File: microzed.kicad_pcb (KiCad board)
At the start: 10 copper layers, 60 x 100 mm, 333 parts, among them IC1 XC7Z020-1CLG484C, IC2 RTL8211E-VL-CG, J1 640456-3, J2 10104111-0001LF, J3 L829-1J1T-43, J4 Micro_SD_Card_Det_Hirose_DM3AT, J5 10104111-0001LF, J6 BSH-090-01-X-D-A, J7 BSH-090-01-X-D-A, Q1 MMBT3904, Q2 MMBT3904, SW1 SW_Push, U1 TLV62130RGTR, U10 MT41K256M16TW, U11 MT25QL128ABA8E12-1SIT, U12 USB3320C-EZK, U13 ASDMB-24.000MHZ-LC-T, U14 ASDMB-25.000MHZ-LC-T, U15 TXS02612RTWR, U16 CP2104-F03-GM, U2 TLV62130RGTR, U3 TLV62130RGTR, U4 TLV62130RGTR, U5 TLV62130RGTR, U6 ASDMB-33.333MHZ-LC-T, U7 TPS51206DSQR, U8 REF3012, U9 MT41K256M16TW

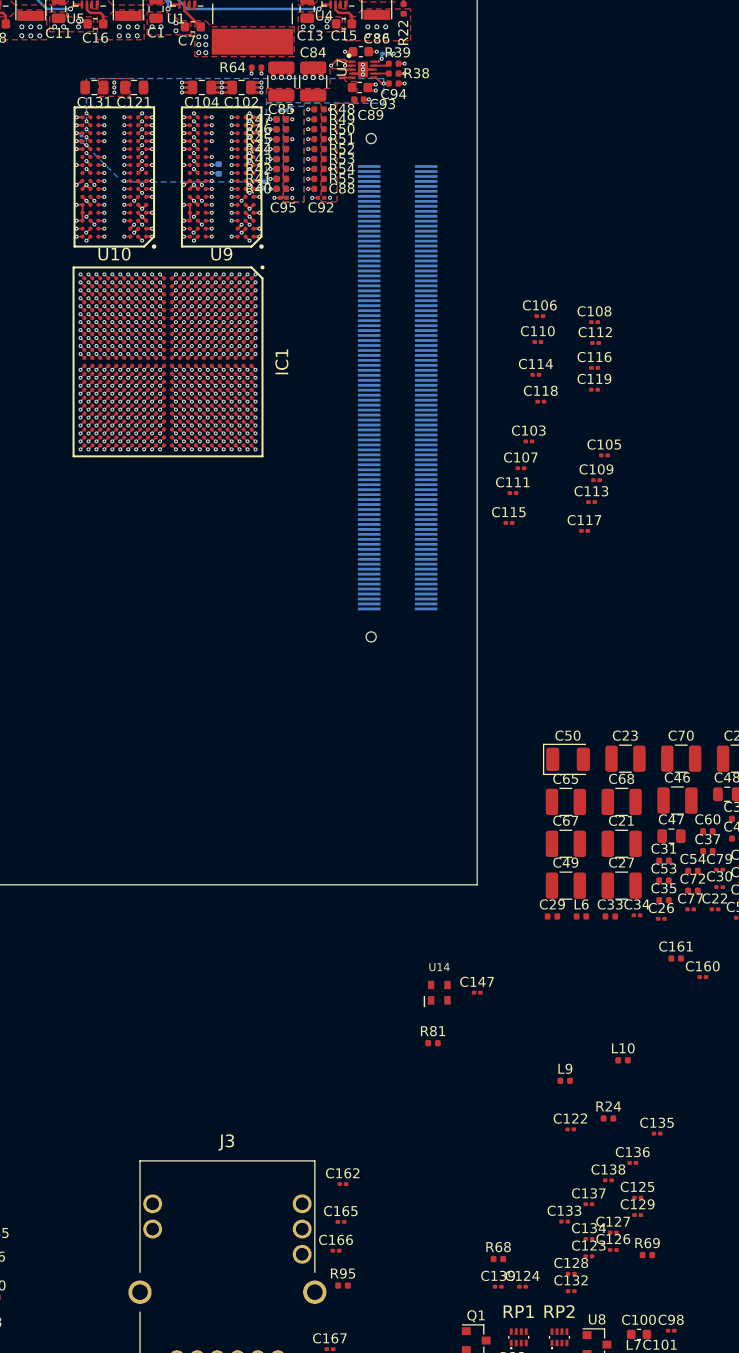
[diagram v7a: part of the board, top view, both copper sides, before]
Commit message: memory capacitor position done.
Signed-off-by: Yi Qingliang <niqingliang2003@gmail.com>
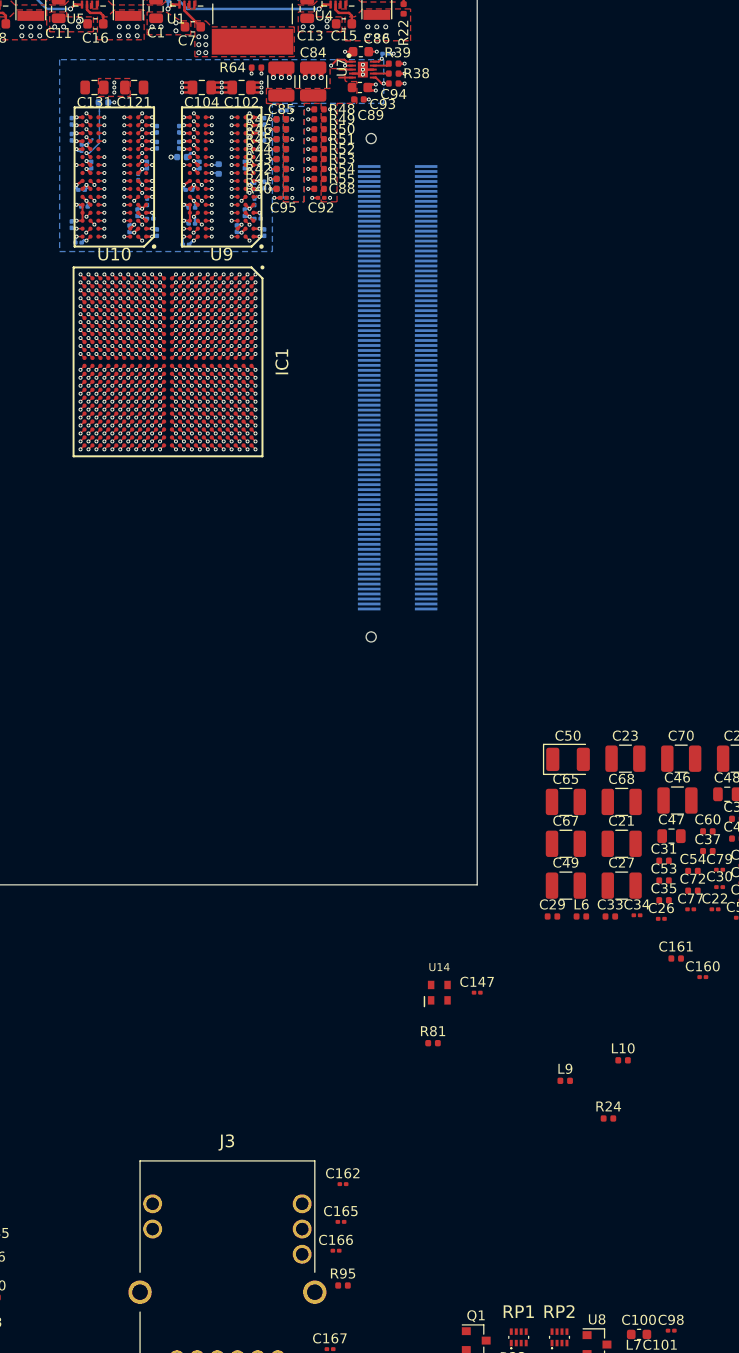
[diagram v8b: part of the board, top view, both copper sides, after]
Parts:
- C103, C105, C106, C107, C108, C109, C110, C111, C112, C113, C114, C115, C116, C117, C118, C119, C122, C123, C124, C125, C126, C127, C128, C129, C132, C133, C134, C135, C136, C137, C138, C139, R68, R69: moved to B.Cu
- moved R69 128.2 mm to (-7.60, 21.3)
- moved C123 125.5 mm to (-10.8, 23.2), turned to 90 degrees
- moved C132 121.0 mm to (-3.20, 27.6), turned to 270 degrees
- moved C128 120.9 mm to (-2.20, 25.6), turned to 270 degrees
- moved C124 120.9 mm to (-8.80, 27.6), turned to 270 degrees
- moved C133 117.3 mm to (-2.20, 24.0), turned to 270 degrees
- moved C126 116.6 mm to (-10.8, 33.6), turned to 270 degrees
- moved C127 116.1 mm to (-9.50, 31.8)
- moved C125 115.8 mm to (-9.80, 30.1)
- moved R68 115.3 mm to (0.30, 26.8), turned to 180 degrees
- moved C134 113.4 mm to (-3.20, 31.3), turned to 270 degrees
- moved C139 113.0 mm to (-2.90, 33.0)
- moved C129 112.8 mm to (-10.1, 35.4), turned to 180 degrees
- moved C122 111.7 mm to (-10.8, 24.8), turned to 90 degrees
- moved C137 109.6 mm to (-4.20, 32.4), turned to 90 degrees
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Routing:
- net GND: track 93.5 -> 112.4 mm, vias 171 -> 173
- net VCCO_DDR: track 46.8 -> 63.6 mm
- net Net-(R69-Pad1): track 0.57 -> 6.37 mm
- net Net-(R68-Pad1): track 0.57 -> 1.45 mm
- net VTTREF: track 6.47 -> 7.08 mm
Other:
- net class DDRSignal: clearance 0.2 -> 0.1
- net class Default: clearance 0.2 -> 0.1
- rule trace_clearance: 0.2 -> 0.1
